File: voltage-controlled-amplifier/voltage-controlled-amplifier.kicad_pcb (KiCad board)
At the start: 2 copper layers, 50.5 x 108.5 mm, 31 parts, among them J1 Power, J10 Output 2, J2 Power, J3 Pot, J4 Input 1, J5 CV 1, J6 Output 1, J7 Pot, J8 Input 2, J9 CV 2, U1 LM13700

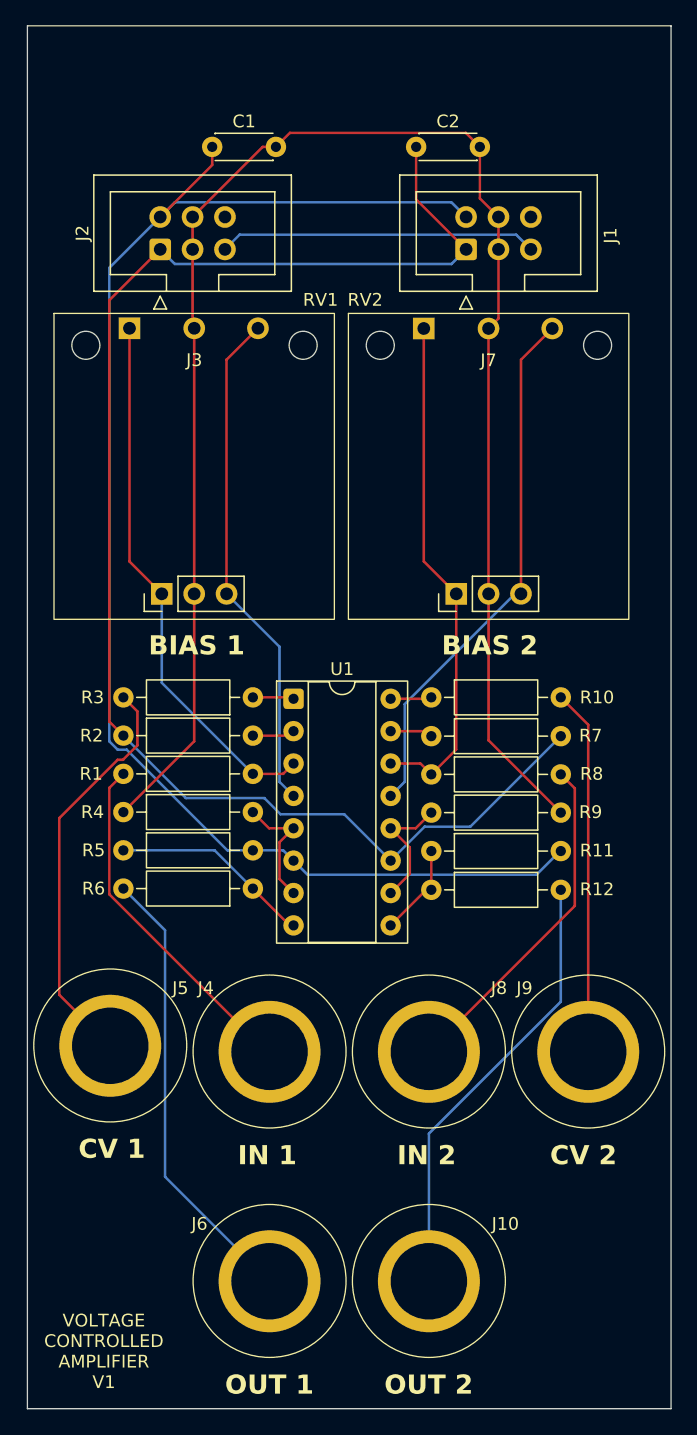
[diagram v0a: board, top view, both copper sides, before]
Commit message: Buffer output of vca
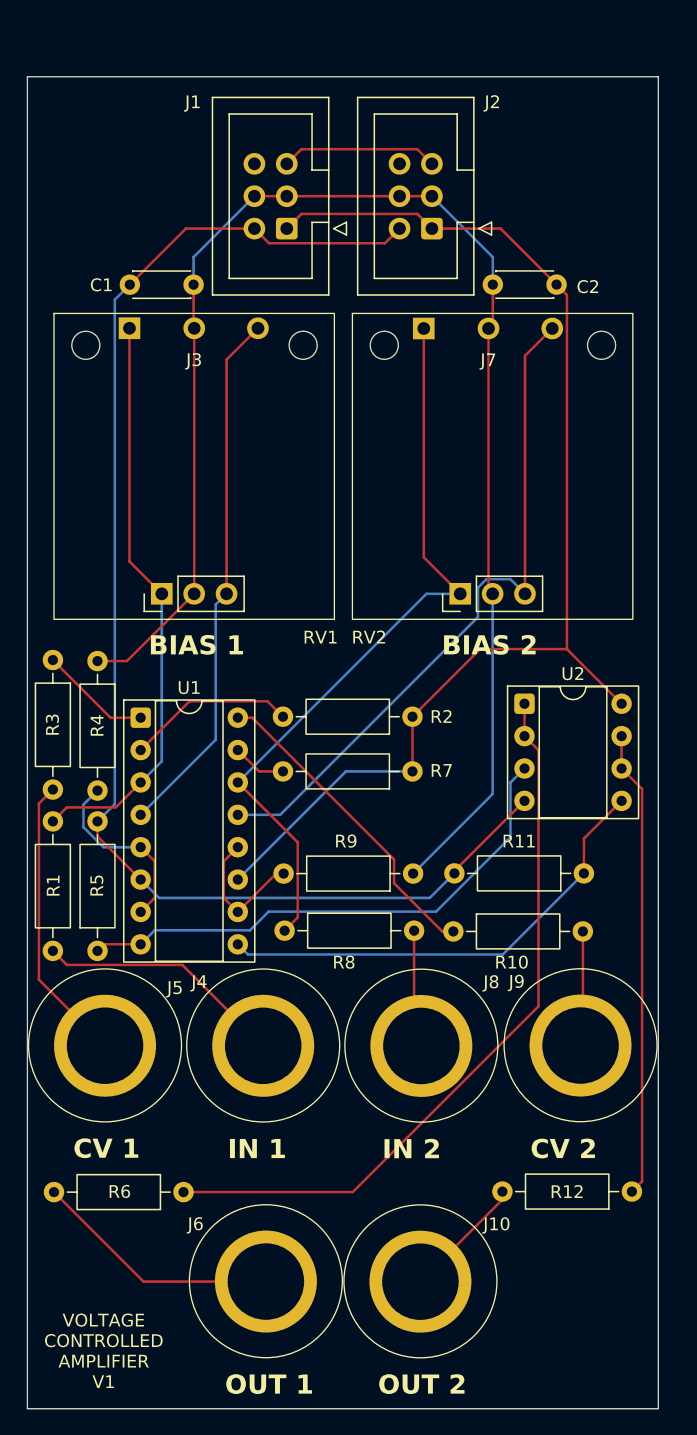
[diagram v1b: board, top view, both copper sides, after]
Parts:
- added U2: TL072, Package_DIP:DIP-8_W7.62mm_Socket, F.Cu at (89.0, 94.7)
- moved R12 28.4 mm to (97.4, 133.0), turned to 180 degrees
- moved R6 24.4 mm to (62.2, 133.0)
- moved R2 22.7 mm to (80.2, 95.7), turned to 180 degrees
- moved J2 21.4 mm to (81.7, 57.4), turned to 180 degrees
- moved R10 18.4 mm to (83.4, 112.6)
- moved R8 16.8 mm to (70.2, 112.5)
- moved R1 16.1 mm to (52.0, 103.9), turned to -90 degrees
- moved R3 16.0 mm to (52.0, 91.3), turned to -90 degrees
- moved J1 14.2 mm to (70.4, 57.4), turned to 180 degrees
- moved C1 12.6 mm to (58.0, 61.8)
- moved R9 12.5 mm to (80.3, 108.0)
- moved R11 12.1 mm to (93.7, 108.0), turned to 180 degrees
- moved U1 12.1 mm to (58.9, 95.8)
- moved R4 12.0 mm to (55.5, 91.3), turned to -90 degrees
- moved R7 12.0 mm to (80.2, 100.0)
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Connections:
- R11 pad 1: Net-(R11-Pad1) -> Net-(U2B-+)
- R12 pad 1: Net-(R11-Pad1) -> Net-(U2B--)
- R5 pad 1: Net-(R5-Pad1) -> Net-(U2A-+)
- R6 pad 1: Net-(R5-Pad1) -> Net-(U2A--)
- U1 pad 8: Net-(R5-Pad1) -> Net-(U2A-+)
- U1 pad 9: Net-(R11-Pad1) -> Net-(U2B-+)
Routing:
- net Net-(U2A--): track 0.00 -> 58.1 mm
- net Net-(U2A-+): track 0.00 -> 41.9 mm
- net Net-(U2B-+): track 0.00 -> 37.0 mm
- net Net-(U2B--): track 0.00 -> 36.7 mm
- net Net-(J10-Pin_1): track 35.1 -> 9.73 mm
- net 12V: track 117.3 -> 94.8 mm
- net Net-(R10-Pad1): track 3.24 -> 24.9 mm
- net Net-(J7-Pin_1): track 40.4 -> 59.6 mm
- net Net-(J9-Pin_1): track 28.7 -> 10.6 mm
- net Net-(J8-Pin_1): track 27.0 -> 9.29 mm
- net Net-(J6-Pin_1): track 35.6 -> 19.5 mm
- net Net-(R5-Pad1): track 15.8 -> 0.00 mm
- net GND: track 130.3 -> 114.9 mm
- net 5V: track 25.0 -> 12.3 mm
- net Net-(J7-Pin_3): track 42.2 -> 53.7 mm
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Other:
- board size 50.5 x 108.5 mm -> 49.5 x 104.5 mm

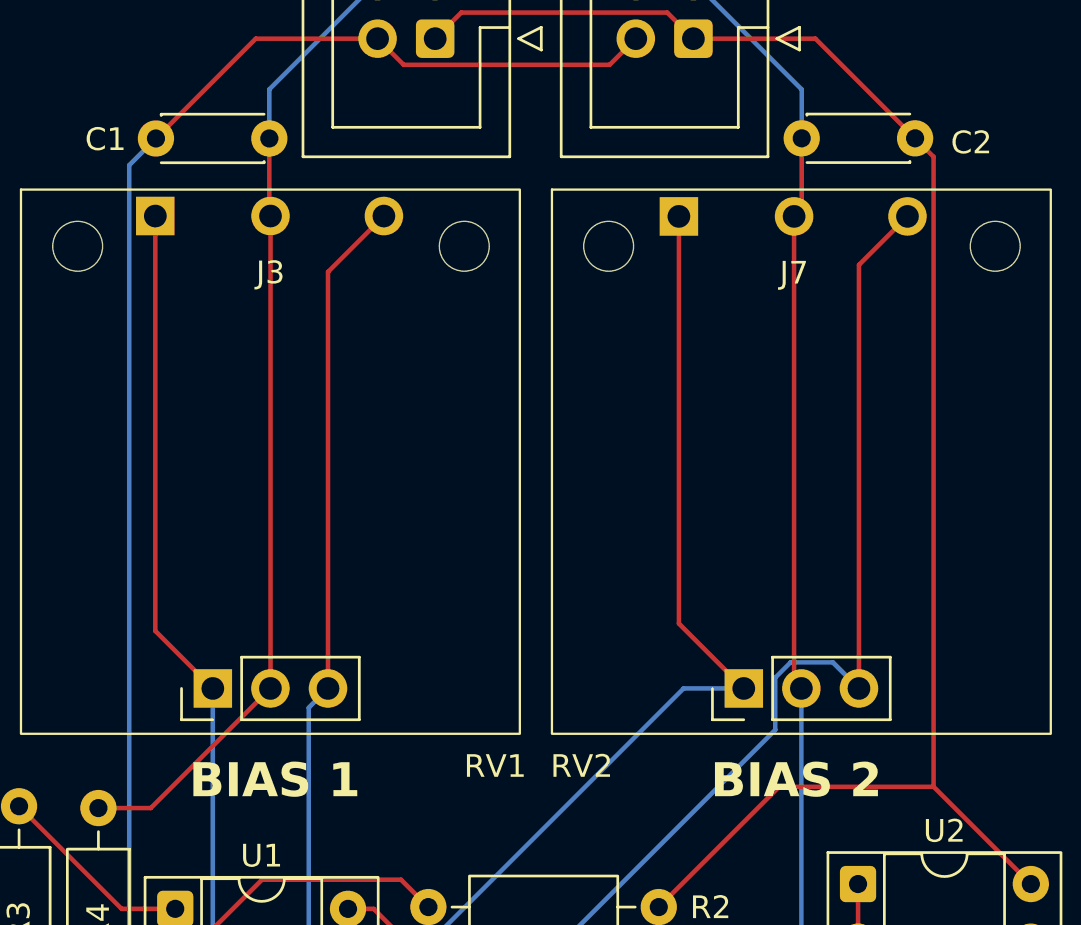
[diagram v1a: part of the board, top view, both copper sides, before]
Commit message: More space for backup pot
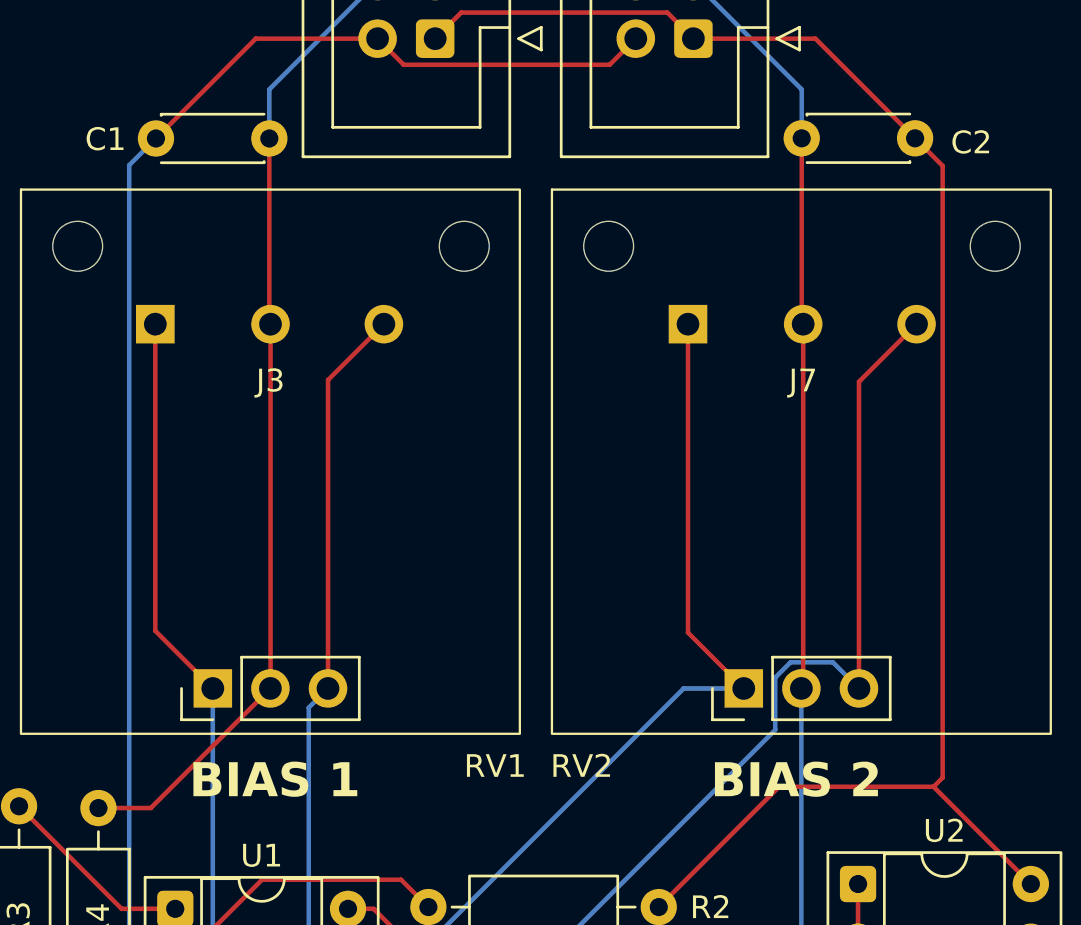
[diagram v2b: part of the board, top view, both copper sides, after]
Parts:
- moved J7 4.77 mm to (86.6, 73.0)
- moved J3 4.77 mm to (63.1, 73.0)
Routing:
- net Net-(J7-Pin_1): track 59.6 -> 54.7 mm
- net Net-(J3-Pin_3): track 42.0 -> 37.2 mm
- net Net-(J3-Pin_1): track 45.5 -> 40.8 mm
- net Net-(J7-Pin_3): track 53.7 -> 49.1 mm
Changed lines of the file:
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@@
 	(footprint "modular2:pot"
 		(layer "F.Cu")
-		(at 86.179291 68.247247)
+		(at 86.58 73)
 		(property "Reference" "J7"
 			(at 0 -0.5 0)
@@
 	(footprint "modular2:pot"
 		(layer "F.Cu")
-		(at 63.089532 68.231407)
+		(at 63.089532 73)
 		(property "Reference" "J3"
 			(at 0 -0.5 0)
@@
 	)
 	(segment
-		(start 86.515656 61.804291)
-		(end 86.515656 64.910882)
+		(start 67.811278 54.86948)
+		(end 70.351278 54.86948)
 		(width 0.2)
 		(layer "F.Cu")
@@
 	)
 	(segment
-		(start 63.089532 65.231407)
-		(end 63.089532 86.060468)
+		(start 63.089532 86.060468)
+		(end 63.085 86.065)
 		(width 0.2)
 		(layer "F.Cu")
@@
 	(segment
 		(start 63.037512 61.811128)
-		(end 63.037512 65.179387)
+		(end 63.037512 69.94798)
 		(width 0.2)
 		(layer "F.Cu")
@@
 	)
 	(segment
-		(start 67.811278 54.86948)
-		(end 70.351278 54.86948)
+		(start 86.58 85.985)
+		(end 86.5 86.065)
 		(width 0.2)
 		(layer "F.Cu")
@@
 	)
 	(segment
-		(start 63.037512 65.179387)
-		(end 63.089532 65.231407)
+		(start 63.085 86.065)
+		(end 57.81 91.34)
 		(width 0.2)
 		(layer "F.Cu")
@@
 	)
 	(segment
-		(start 63.089532 86.060468)
-		(end 63.085 86.065)
+		(start 86.179291 85.744291)
+		(end 86.5 86.065)
 		(width 0.2)
 		(layer "F.Cu")
@@
 	)
 	(segment
-		(start 63.085 86.065)
-		(end 57.81 91.34)
+		(start 79.198158 54.86948)
+		(end 81.738158 54.86948)
 		(width 0.2)
 		(layer "F.Cu")
@@
 	)
 	(segment
-		(start 86.179291 85.744291)
-		(end 86.5 86.065)
+		(start 63.037512 69.94798)
+		(end 63.089532 70)
 		(width 0.2)
 		(layer "F.Cu")
@@
 	)
 	(segment
-		(start 79.198158 54.86948)
-		(end 81.738158 54.86948)
+		(start 70.351278 54.86948)
+		(end 79.198158 54.86948)
 		(width 0.2)
 		(layer "F.Cu")
@@
 	)
 	(segment
-		(start 70.351278 54.86948)
-		(end 79.198158 54.86948)
+		(start 86.515656 69.935656)
+		(end 86.58 70)
 		(width 0.2)
 		(layer "F.Cu")
@@
 	)
 	(segment
-		(start 86.515656 64.910882)
-		(end 86.179291 65.247247)
+		(start 86.58 70)
+		(end 86.58 85.985)
+		(width 0.2)
+		(layer "F.Cu")
+		(net 2)
+	)
+	(segment
+		(start 63.089532 70)
+		(end 63.089532 86.060468)
 		(width 0.2)
 		(layer "F.Cu")
@@
 	)
 	(segment
-		(start 86.179291 65.247247)
-		(end 86.179291 85.744291)
+		(start 86.515656 61.804291)
+		(end 86.515656 69.935656)
 		(width 0.2)
 		(layer "F.Cu")
@@
 	)
 	(segment
-		(start 91.515656 61.804291)
-		(end 92.330291 62.618926)
+		(start 70.351278 57.40948)
+		(end 71.502278 56.25848)
 		(width 0.2)
 		(layer "F.Cu")
@@
 	)
 	(segment
-		(start 70.351278 57.40948)
-		(end 71.502278 56.25848)
+		(start 80.211822 95.706162)
+		(end 85.517693 90.400291)
 		(width 0.2)
 		(layer "F.Cu")
@@
 	)
 	(segment
-		(start 80.211822 95.706162)
-		(end 85.517693 90.400291)
+		(start 92.731 63.019635)
+		(end 92.731 89.999582)
 		(width 0.2)
 		(layer "F.Cu")
@@
 	)
 	(segment
-		(start 92.330291 62.618926)
+		(start 92.731 89.999582)
 		(end 92.330291 90.400291)
 		(width 0.2)
@@
 	)
 	(segment
+		(start 91.515656 61.804291)
+		(end 92.731 63.019635)
+		(width 0.2)
+		(layer "F.Cu")
+		(net 3)
+	)
+	(segment
 		(start 74.992328 100)
 		(end 66.507798 108.48453)
@@
 	)
 	(segment
-		(start 65.625 67.695939)
+		(start 65.625 72.464532)
 		(end 65.625 86.065)
 		(width 0.2)
@@
 	)
 	(segment
-		(start 68.089532 65.231407)
-		(end 65.625 67.695939)
+		(start 68.089532 70)
+		(end 65.625 72.464532)
 		(width 0.2)
 		(layer "F.Cu")
@@
 	)
 	(segment
-		(start 58.009532 65.231407)
-		(end 58.009532 83.529532)
+		(start 58.009532 83.529532)
+		(end 60.545 86.065)
 		(width 0.2)
 		(layer "F.Cu")
@@
 	)
 	(segment
-		(start 58.009532 83.529532)
-		(end 60.545 86.065)
+		(start 58.009532 70)
+		(end 58.009532 83.529532)
 		(width 0.2)
 		(layer "F.Cu")
@@
 	)
 	(segment
-		(start 81.099291 83.204291)
-		(end 83.96 86.065)
+		(start 71.204025 105.560757)
+		(end 66.507798 100.86453)
 		(width 0.2)
 		(layer "F.Cu")
@@
 	)
 	(segment
-		(start 71.204025 105.560757)
-		(end 66.507798 100.86453)
+		(start 81.5 83.605)
+		(end 83.96 86.065)
 		(width 0.2)
 		(layer "F.Cu")
@@
 	)
 	(segment
-		(start 71.204025 111.469738)
-		(end 71.204025 105.560757)
+		(start 81.5 70)
+		(end 81.5 83.605)
 		(width 0.2)
 		(layer "F.Cu")
@@
 	)
 	(segment
-		(start 81.099291 65.247247)
-		(end 81.099291 83.204291)
+		(start 71.204025 111.469738)
+		(end 71.204025 105.560757)
 		(width 0.2)
 		(layer "F.Cu")
@@
 	)
 	(segment
-		(start 91.179291 65.247247)
-		(end 89.04 67.386538)
+		(start 89.04 72.54)
+		(end 89.04 86.065)
 		(width 0.2)
 		(layer "F.Cu")
@@
 	)
 	(segment
-		(start 89.04 67.386538)
-		(end 89.04 86.065)
+		(start 91.58 70)
+		(end 89.04 72.54)
 		(width 0.2)
 		(layer "F.Cu")

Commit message: Various improvements
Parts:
- added C3: 100nf, Capacitor_THT:C_Disc_D4.3mm_W1.9mm_P5.00mm, F.Cu at (91.6, 91.8)
- added C4: 100nf, Capacitor_THT:C_Disc_D4.3mm_W1.9mm_P5.00mm, F.Cu at (86.2, 102.3)
- moved C2 60.5 mm to (56.2, 114.1), turned to 180 degrees
- moved C1 49.8 mm to (74.2, 108.9), turned to 180 degrees
- moved R1 2.29 mm to (52.1, 101.6)
- moved R5 2.28 mm to (55.5, 111.8)
- moved R4 2.09 mm to (55.5, 89.3)
- moved R9 2.07 mm to (80.3, 105.9)
- moved R3 2.00 mm to (52.1, 89.3)
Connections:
- C1 pad 1: -12V -> GND
- C1 pad 2: GND -> 12V
- C2 pad 1: GND -> -12V
- C2 pad 2: 12V -> GND
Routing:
- net -12V: track 107.0 -> 145.0 mm
- net GND: track 115.1 -> 150.4 mm
- net Net-(J7-Pin_1): track 54.7 -> 59.9 mm
- net Net-(R9-Pad2): track 10.8 -> 5.99 mm
- net 12V: track 95.1 -> 98.4 mm
- net Net-(J5-Pin_1): track 22.7 -> 24.7 mm
- net Net-(J4-Pin_1): track 19.6 -> 20.4 mm
- net Net-(R3-Pad1): track 8.76 -> 9.49 mm
- net Net-(U2A-+): track 41.9 -> 42.5 mm
- net Net-(R4-Pad2): track 14.5 -> 13.9 mm

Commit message: Various fixes
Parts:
- moved R4 30.8 mm to (86.2, 92.5), turned to 180 degrees
- moved R3 21.2 mm to (73.1, 92.5), turned to 180 degrees
- moved R5 8.22 mm to (55.5, 103.6)
- moved C2 5.60 mm to (56.0, 108.5), turned to -90 degrees
- moved R1 1.79 mm to (52.0, 103.4)
- moved J1 1.61 mm to (70.4, 55.8)
- moved J2 1.61 mm to (81.7, 55.8)
- moved J3 1.61 mm to (63.1, 71.4)
- moved J7 1.61 mm to (86.6, 71.4)
- moved RV1 1.61 mm to (62.1, 76.5)
- moved RV2 1.61 mm to (85.5, 76.5)
- moved F1 0.72 mm to (92.5, 51.5)
- moved F2 0.72 mm to (57.0, 51.5)
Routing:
- net -12V: track 145.0 -> 117.0 mm
- net Net-(R4-Pad2): track 13.9 -> 29.0 mm
- net Net-(J4-Pin_1): track 20.4 -> 29.8 mm
- net Net-(U2A-+): track 42.5 -> 49.7 mm
- net Net-(J5-Pin_1): track 24.7 -> 31.8 mm
- net Net-(R3-Pad1): track 9.49 -> 15.6 mm
- net Net-(R9-Pad2): track 5.99 -> 9.60 mm
- net 12V: track 98.4 -> 96.2 mm
- net Net-(J3-Pin_1): track 40.6 -> 42.4 mm
- net Net-(J7-Pin_3): track 49.1 -> 47.5 mm
- net Net-(J3-Pin_3): track 37.2 -> 38.8 mm
- net Net-(U1C-DIODE_BIAS): track 13.2 -> 12.2 mm
- net Net-(J7-Pin_1): track 59.9 -> 60.8 mm
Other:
- board size 49.5 x 104.5 mm -> 49.5 x 105.5 mm

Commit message: Update gerbers
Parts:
- added G***: LOGO, modular2:ibis-small, F.Cu at (95.2, 144.7)

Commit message: Vca fixes
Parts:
- R11, R5: value 5k -> 5.1k
- moved J2 5.68 mm to (79.2, 50.7), turned to 0 degrees
- moved F4 0.43 mm to (56.9, 142.7)
- moved F3 0.42 mm to (92.6, 142.7)
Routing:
- net 5V: track 12.3 -> 21.8 mm
- net -12V: track 117.0 -> 121.5 mm
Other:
- board text added: "VCA"
